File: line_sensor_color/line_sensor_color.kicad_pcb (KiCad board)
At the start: 2 copper layers, 99.1 x 72.4 mm, 65 parts, among them SW1 SW_DIP_x03, SW2 SW_DIP_x03, SW3 SW_DIP_x03, SW4 SW_DIP_x03, SW5 SW_DIP_x03, SW6 SW_DIP_x03, U1 XH_2, U2 XH_2, U3 XH_2, U4 NJM7800SDL1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

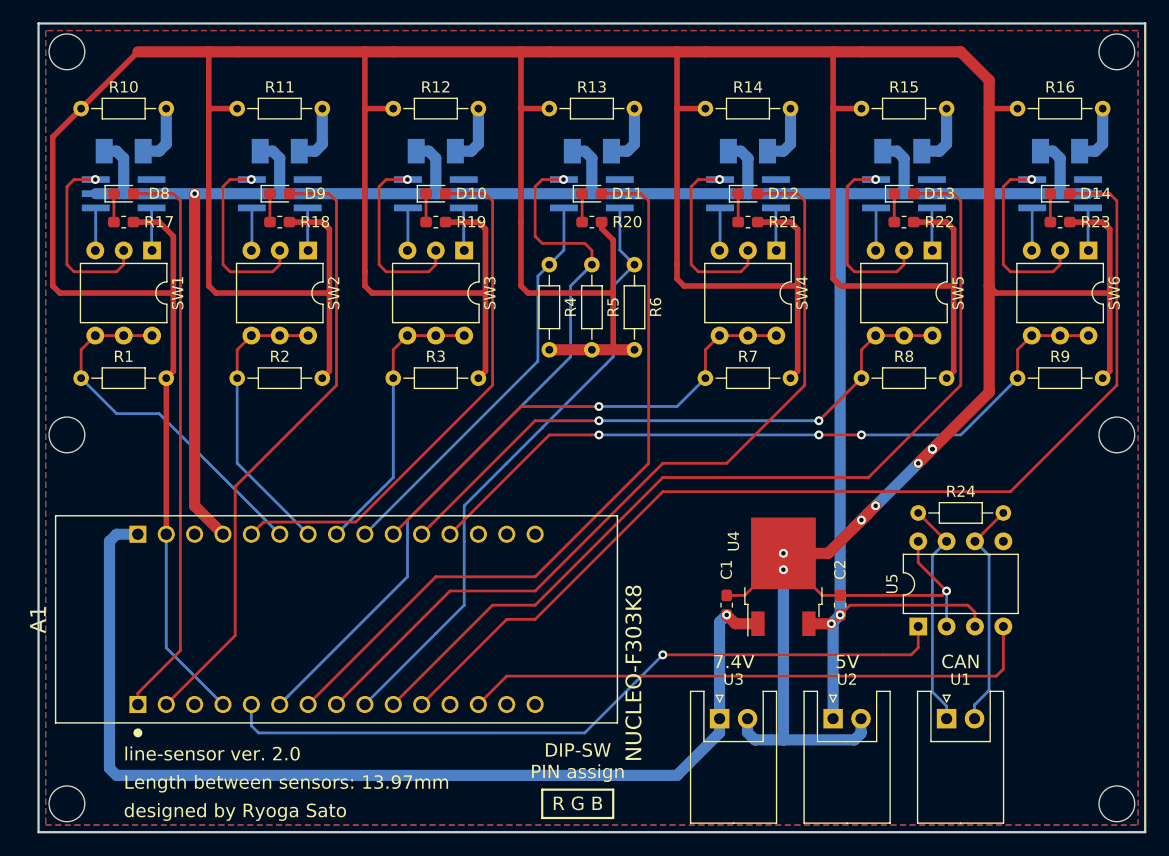
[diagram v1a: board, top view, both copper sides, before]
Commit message: update: ライブラリの更新
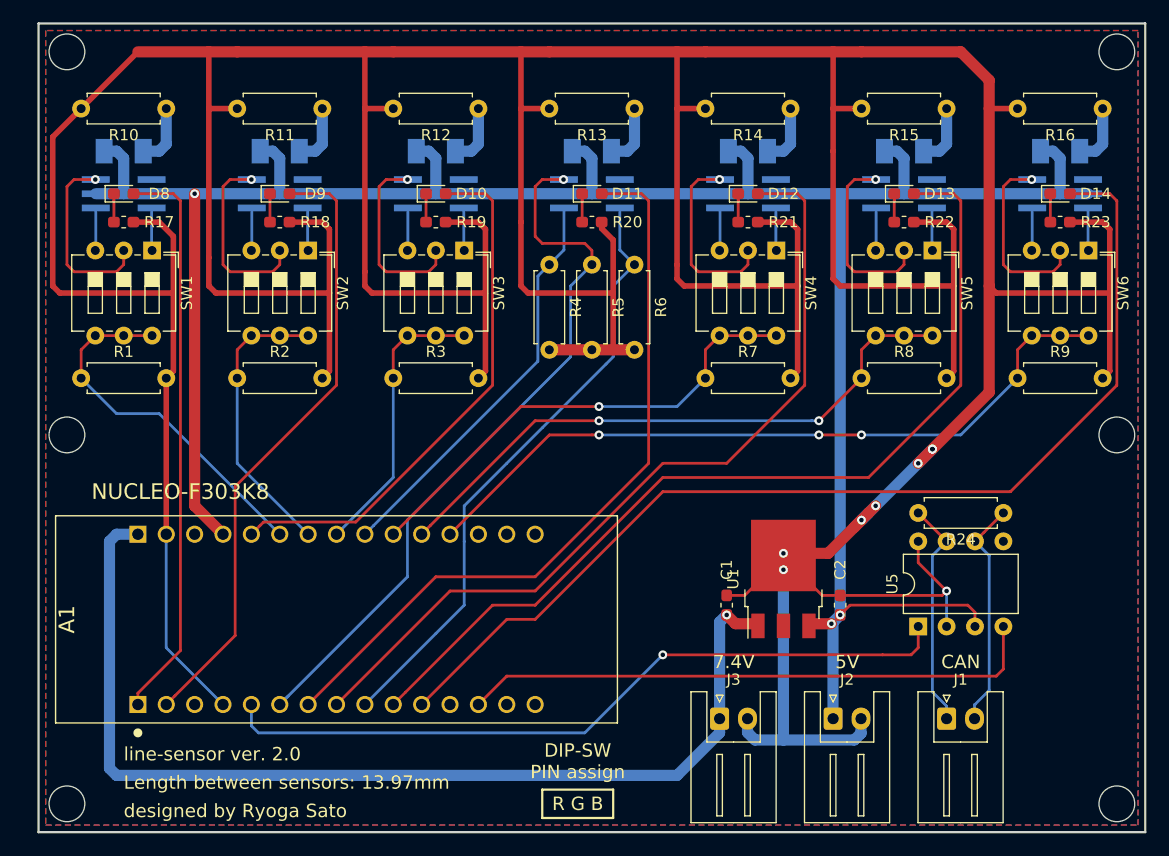
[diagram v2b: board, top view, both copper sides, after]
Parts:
- removed U2, U3: XH_2, MyFootprint:JST_XH_S02B-XH-A_02x2.50mm_Angled
- removed U4: NJM7800SDL1, Package_TO_SOT_SMD:TO-252-2
- added J1: Conn_01x02_Male, Connector_JST:JST_XH_S2B-XH-A_1x02_P2.50mm_Horizontal, F.Cu at (186.7, 119.4)
- added J2: Conn_01x02_Male, Connector_JST:JST_XH_S2B-XH-A_1x02_P2.50mm_Horizontal, F.Cu at (176.5, 119.4)
- added J3: Conn_01x02_Male, Connector_JST:JST_XH_S2B-XH-A_1x02_P2.50mm_Horizontal, F.Cu at (166.4, 119.4)
- R1, R10, R11, R12, R13, R14, R15, R16, R2, R24, R3, R4, R5, R6, R7, R8, R9: footprint Resistor_THT:R_Axial_DIN0204_L3.6mm_D1.6mm_P7.62mm_Horizontal -> Resistor_THT:R_Axial_DIN0207_L6.3mm_D2.5mm_P7.62mm_Horizontal
- SW1, SW2, SW3, SW4, SW5, SW6: footprint Package_DIP:DIP-6_W7.62mm -> Button_Switch_THT:SW_DIP_SPSTx03_Slide_6.7x9.18mm_W7.62mm_P2.54mm_LowProfile
- U1: value XH_2 -> NJM7805SDL1-MyComponent; footprint MyFootprint:JST_XH_S02B-XH-A_02x2.50mm_Angled -> Package_TO_SOT_SMD:TO-252-3_TabPin2
- moved U1 19.2 mm to (172.1, 106.9), turned to 90 degrees
- moved D6 0.16 mm to (182.9, 68.6)
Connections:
- U1 pad 1: CAN_H -> +BATT
- U1 pad 2: CAN_L -> GND
